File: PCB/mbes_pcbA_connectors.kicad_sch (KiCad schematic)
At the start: 14 parts

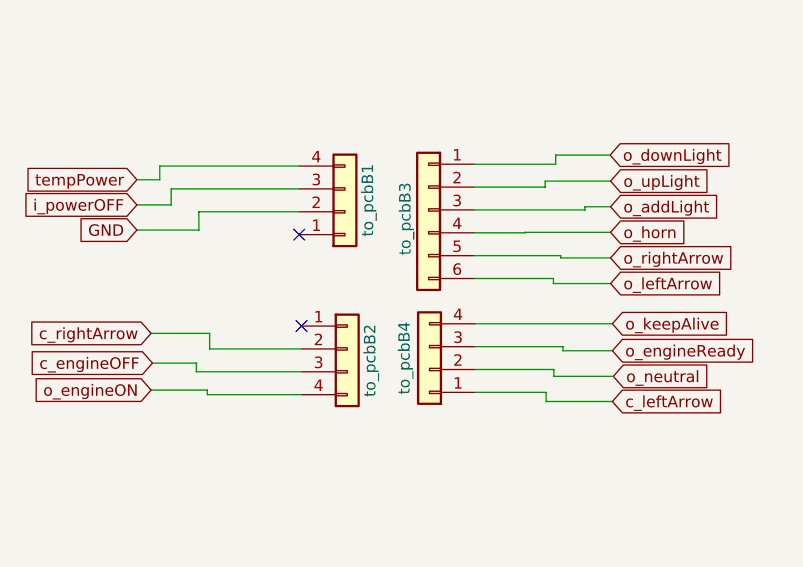
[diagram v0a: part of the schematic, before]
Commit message: Wrong connectors sizes fixed
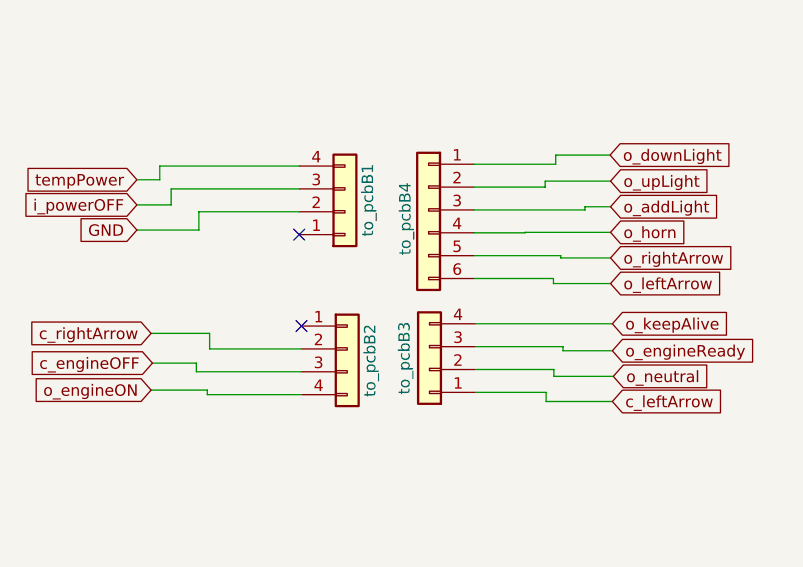
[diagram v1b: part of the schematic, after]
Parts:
- renumbered to_pcbB4 to to_pcbB3, to_pcbB3 to to_pcbB4
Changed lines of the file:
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@@
 		(on_board yes)
 		(dnp no)
-		(property "Reference" "to_pcbB4"
+		(property "Reference" "to_pcbB3"
 			(at 202.184 124.968 90)
 			(effects
@@
 			(project "pcb-a"
 				(path "/709d0967-afe5-49d3-92a5-d2bb94550bdb/0b22d592-b723-42a2-89dd-bec665c2bd26"
-					(reference "to_pcbB4")
+					(reference "to_pcbB3")
 					(unit 1)
 				)
@@
 		(on_board yes)
 		(dnp no)
-		(property "Reference" "to_pcbB3"
+		(property "Reference" "to_pcbB4"
 			(at 202.2856 113.538 90)
 			(effects
@@
 			(project "pcb-a"
 				(path "/709d0967-afe5-49d3-92a5-d2bb94550bdb/0b22d592-b723-42a2-89dd-bec665c2bd26"
-					(reference "to_pcbB3")
-					(unit 1)
-				)
+					(reference "to_pcbB4")
+					(unit 1)
+				)

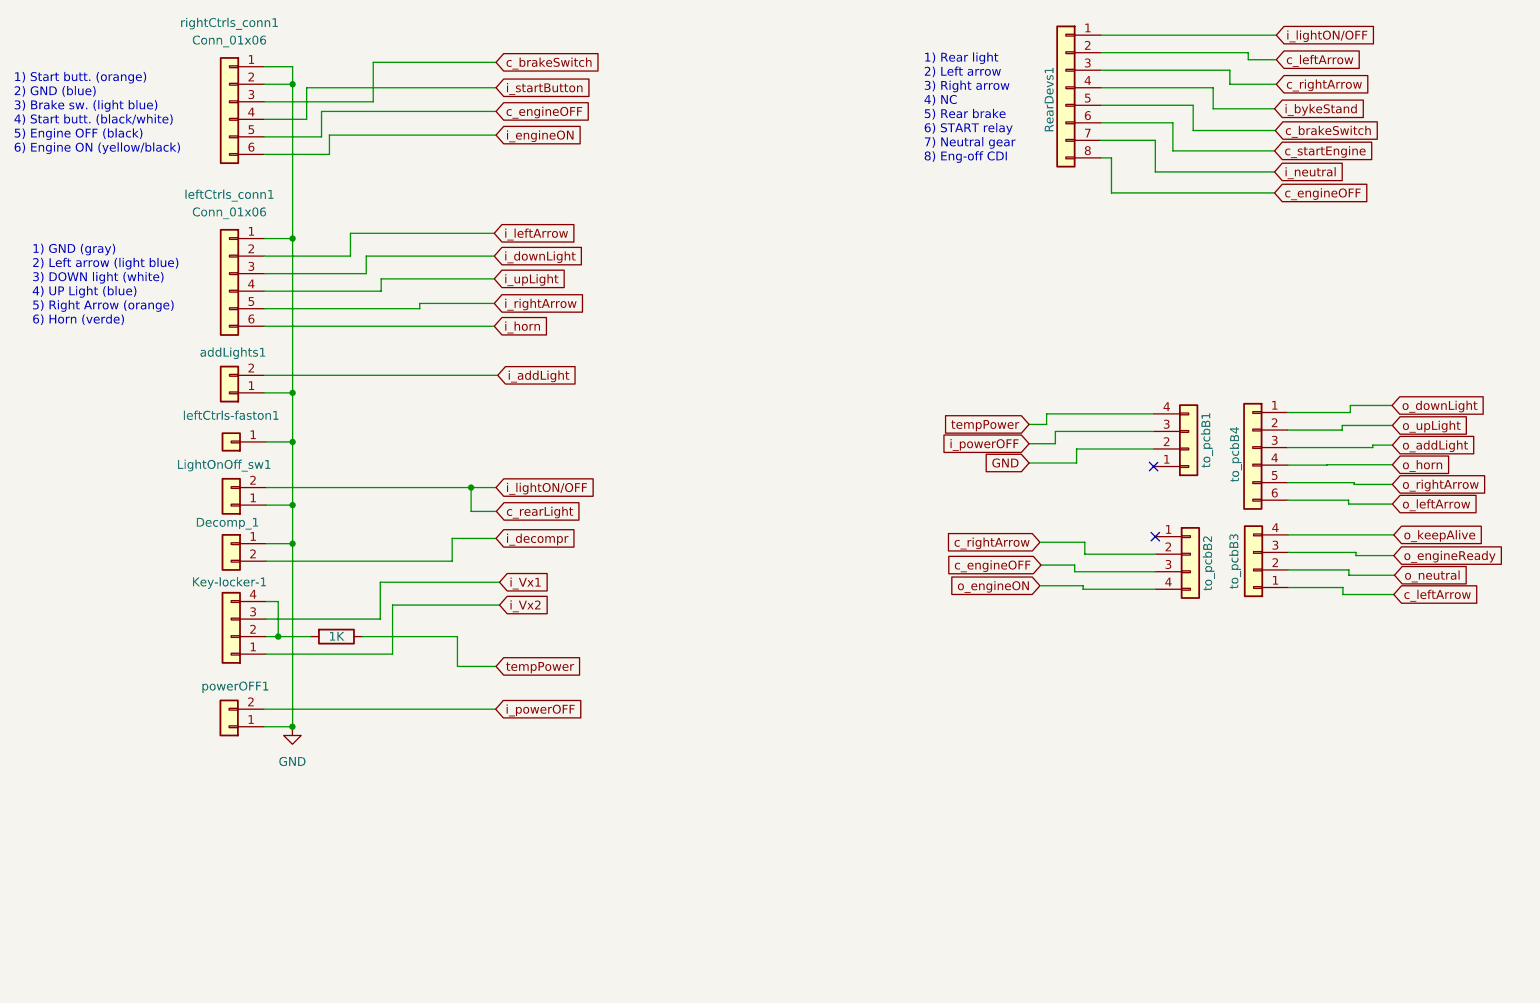
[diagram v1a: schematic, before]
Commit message: Parking button added and Horn management removed
Horn is connected directly to the power PCB
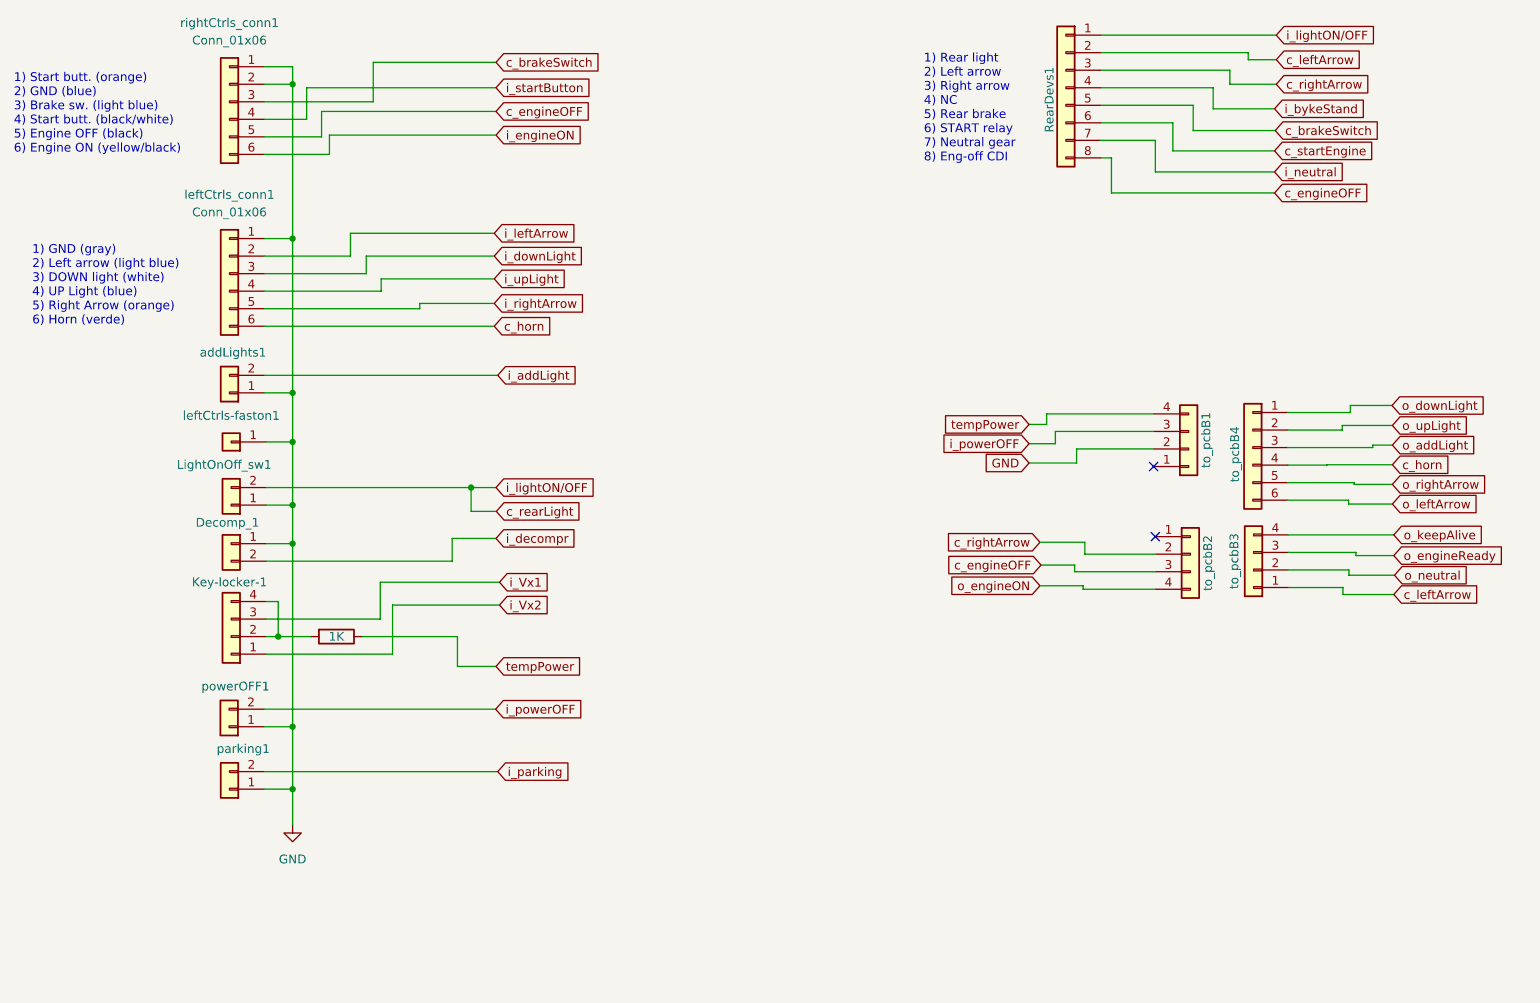
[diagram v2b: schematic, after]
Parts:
- added parking1: Conn_01x02, Connector_Wire:SolderWire-0.15sqmm_1x02_P4mm_D0.5mm_OD1.5mm, symbol Connector_Generic:Conn_01x02
- R1: footprint Resistor_THT:R_Axial_DIN0207_L6.3mm_D2.5mm_P7.62mm_Horizontal -> Resistor_THT:R_Axial_DIN0204_L3.6mm_D1.6mm_P5.08mm_Horizontal
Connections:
- net o_horn is gone; now on net c_horn: to_pcbB4.4 (Pin_4)
- net GND: now also parking1.1 (Pin_1)
- net i_horn renamed c_horn
- new net i_parking: parking1.2 (Pin_2)
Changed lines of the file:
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@@
 	)
 	(junction
+		(at 65.786 148.9456)
+		(diameter 0)
+		(color 0 0 0 0)
+	)
+	(junction
 		(at 65.786 122.428)
 		(diameter 0)
@@
 	)
 	(junction
-		(at 65.7606 148.9456)
+		(at 65.786 157.988)
 		(diameter 0)
 		(color 0 0 0 0)
@@
 	(wire
 		(pts
+			(xy 61.722 155.448) (xy 95.504 155.448)
+		)
+		(stroke
+			(width 0)
+			(type default)
+		)
+	)
+	(wire
+		(pts
 			(xy 208.1276 62.5856) (xy 196.2404 62.5856)
 		)
@@
 	(wire
 		(pts
+			(xy 61.722 157.988) (xy 65.786 157.988)
+		)
+		(stroke
+			(width 0)
+			(type default)
+		)
+	)
+	(wire
+		(pts
 			(xy 219.5576 113.8428) (xy 225.0948 113.8428)
 		)
@@
 	(wire
 		(pts
+			(xy 65.786 163.068) (xy 65.786 157.988)
+		)
+		(stroke
+			(width 0)
+			(type default)
+		)
+	)
+	(wire
+		(pts
 			(xy 209.9564 113.5888) (xy 219.5576 113.5888)
 		)
@@
 	(wire
 		(pts
-			(xy 65.7606 148.9456) (xy 65.786 148.9456)
-		)
-		(stroke
-			(width 0)
-			(type default)
-		)
-	)
-	(wire
-		(pts
 			(xy 180.2892 129.032) (xy 190.754 129.032)
 		)
@@
 	(wire
 		(pts
-			(xy 61.6712 148.9456) (xy 65.7606 148.9456)
+			(xy 61.6712 148.9456) (xy 65.786 148.9456)
 		)
 		(stroke
@@
 	(wire
 		(pts
+			(xy 65.786 157.988) (xy 65.786 148.9456)
+		)
+		(stroke
+			(width 0)
+			(type default)
+		)
+	)
+	(wire
+		(pts
 			(xy 201.549 53.848) (xy 201.549 55.88)
 		)
@@
 		)
 	)
-	(global_label "o_horn"
+	(global_label "c_horn"
 		(shape input)
 		(at 225.0948 110.998 0)
@@
 		)
 		(property "Intersheetrefs" "${INTERSHEET_REFS}"
-			(at 225.0948 110.998 0)
+			(at 234.3694 110.998 0)
 			(effects
 				(font
 					(size 1.27 1.27)
 				)
+				(justify left)
 				(hide yes)
 			)
 		)
 		(property "Riferimenti inter-foglio" "${INTERSHEET_REFS}"
-			(at 233.8579 110.9186 0)
+			(at 225.0948 113.1888 0)
 			(effects
 				(font
@@
 		)
 	)
-	(global_label "i_horn"
+	(global_label "c_horn"
 		(shape input)
 		(at 94.996 90.932 0)
@@
 		)
 		(property "Intersheetrefs" "${INTERSHEET_REFS}"
-			(at 94.996 90.932 0)
+			(at 104.2706 90.932 0)
 			(effects
 				(font
 					(size 1.27 1.27)
 				)
+				(justify left)
 				(hide yes)
 			)
 		)
 		(property "Riferimenti inter-foglio" "${INTERSHEET_REFS}"
-			(at 103.2148 90.8526 0)
+			(at 94.996 93.1228 0)
 			(effects
 				(font
@@
 		)
 	)
+	(global_label "i_parking"
+		(shape input)
+		(at 95.504 155.448 0)
+		(fields_autoplaced yes)
+		(effects
+			(font
+				(size 1.27 1.27)
+			)
+			(justify left)
+		)
+		(property "Intersheetrefs" "${INTERSHEET_REFS}"
+			(at 107.0767 155.448 0)
+			(effects
+				(font
+					(size 1.27 1.27)
+				)
+				(justify left)
+				(hide yes)
+			)
+		)
+		(property "Riferimenti inter-foglio" "${INTERSHEET_REFS}"
+			(at 95.504 157.6388 0)
+			(effects
+				(font
+					(size 1.27 1.27)
+				)
+				(justify left)
+				(hide yes)
+			)
+		)
+	)
 	(global_label "c_rearLight"
 		(shape input)
@@
 	(symbol
 		(lib_id "power:GND")
-		(at 65.7606 148.9456 0)
+		(at 65.786 163.068 0)
 		(unit 1)
 		(exclude_from_sim no)
@@
 		(fields_autoplaced yes)
 		(property "Reference" "#PWR0108"
-			(at 65.7606 155.2956 0)
+			(at 65.786 169.418 0)
 			(effects
 				(font
@@
 		)
 		(property "Value" "GND"
-			(at 65.7606 154.0256 0)
+			(at 65.786 168.148 0)
 			(effects
 				(font
@@
 		)
 		(property "Footprint" ""
-			(at 65.7606 148.9456 0)
+			(at 65.786 163.068 0)
 			(effects
 				(font
@@
 		)
 		(property "Datasheet" ""
-			(at 65.7606 148.9456 0)
+			(at 65.786 163.068 0)
 			(effects
 				(font
@@
 		)
 		(property "Description" ""
-			(at 65.7606 148.9456 0)
+			(at 65.786 163.068 0)
 			(effects
 				(font
@@
 	)
 	(symbol
+		(lib_id "Connector_Generic:Conn_01x02")
+		(at 56.642 157.988 180)
+		(unit 1)
+		(exclude_from_sim no)
+		(in_bom yes)
+		(on_board yes)
+		(dnp no)
+		(property "Reference" "parking1"
+			(at 62.484 152.146 0)
+			(effects
+				(font
+					(size 1.27 1.27)
+				)
+				(justify left)
+			)
+		)
+		(property "Value" "Conn_01x02"
+			(at 55.3721 160.528 90)
+			(effects
+				(font
+					(size 1.27 1.27)
+				)
+				(justify left)
+				(hide yes)
+			)
+		)
+		(property "Footprint" "Connector_Wire:SolderWire-0.15sqmm_1x02_P4mm_D0.5mm_OD1.5mm"
+			(at 56.642 157.988 0)
+			(effects
+				(font
+					(size 1.27 1.27)
+				)
+				(hide yes)
+			)
+		)
+		(property "Datasheet" "~"
+			(at 56.642 157.988 0)
+			(effects
+				(font
+					(size 1.27 1.27)
+				)
+				(hide yes)
+			)
+		)
+		(property "Description" ""
+			(at 56.642 157.988 0)
+			(effects
+				(font
+					(size 1.27 1.27)
+				)
+				(hide yes)
+			)
+		)
+		(pin "1"
+		)
+		(pin "2"
+		)
+		(instances
+			(project "pcb-a"
+				(path "/709d0967-afe5-49d3-92a5-d2bb94550bdb/0b22d592-b723-42a2-89dd-bec665c2bd26"
+					(reference "parking1")
+					(unit 1)
+				)
+			)
+		)
+	)
+	(symbol
 		(lib_id "Connector_Generic:Conn_01x04")
 		(at 195.834 123.952 0)
@@
 			)
 		)
-		(property "Footprint" "Resistor_THT:R_Axial_DIN0207_L6.3mm_D2.5mm_P7.62mm_Horizontal"
+		(property "Footprint" "Resistor_THT:R_Axial_DIN0204_L3.6mm_D1.6mm_P5.08mm_Horizontal"
 			(at 72.136 134.112 90)
 			(effects

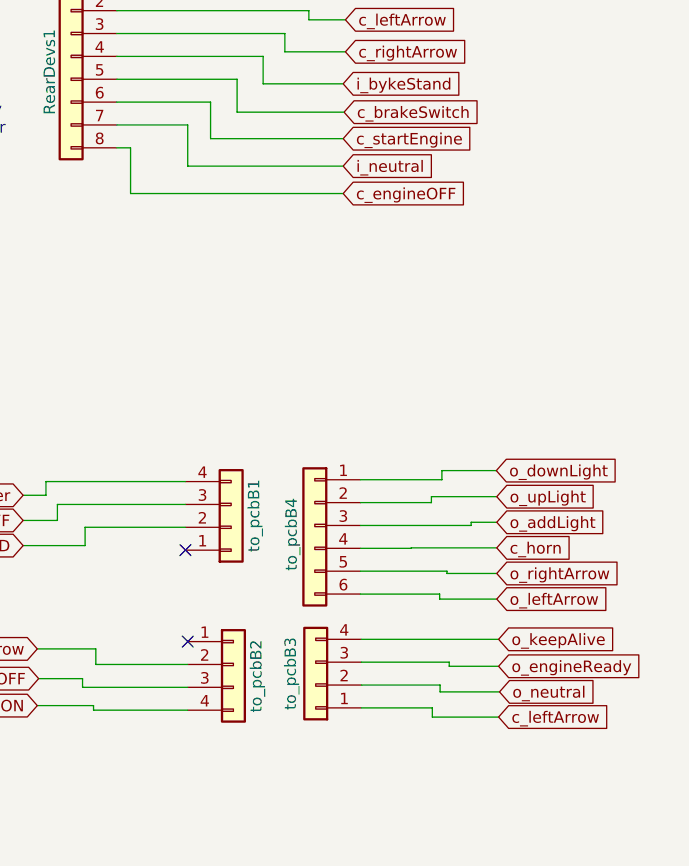
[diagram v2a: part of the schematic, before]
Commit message: o_NEUTRAL is connected directly to the led
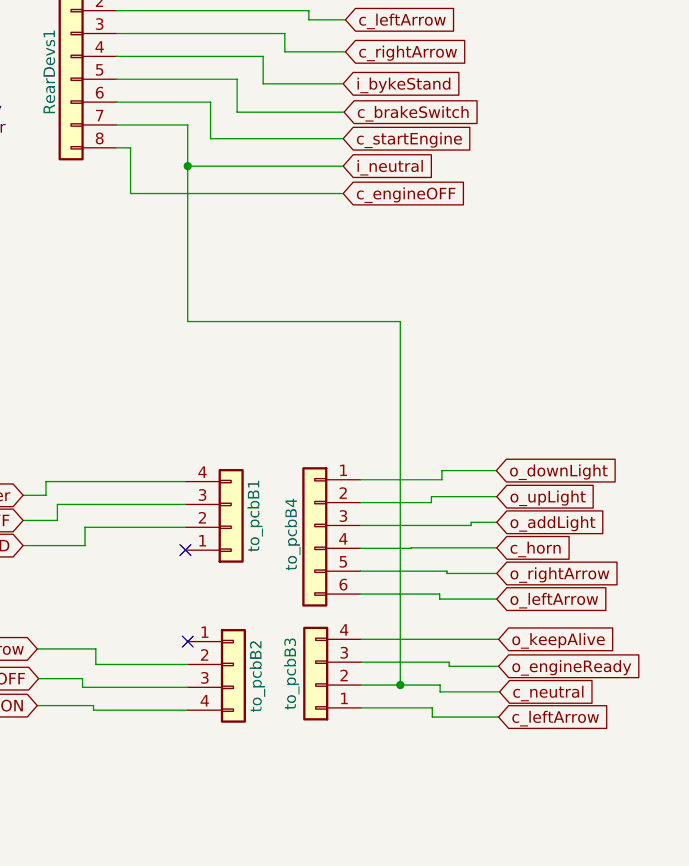
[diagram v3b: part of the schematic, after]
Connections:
- net o_neutral is gone; now on net c_neutral: to_pcbB3.2 (Pin_2)
- net i_neutral renamed c_neutral
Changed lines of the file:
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@@
+	)
+	(junction
+		(at 214.376 126.238)
+		(diameter 0)
+		(color 0 0 0 0)
 	)
 	(junction
@@
 	)
 	(junction
+		(at 190.754 68.58)
+		(diameter 0)
+		(color 0 0 0 0)
+	)
+	(junction
 		(at 91.6432 114.3)
 		(diameter 0)
@@
 	(wire
 		(pts
+			(xy 214.376 126.238) (xy 210.058 126.238)
+		)
+		(stroke
+			(width 0)
+			(type default)
+		)
+	)
+	(wire
+		(pts
 			(xy 180.2892 129.032) (xy 190.754 129.032)
 		)
@@
 	(wire
 		(pts
-			(xy 218.7956 126.238) (xy 210.058 126.238)
+			(xy 214.376 85.852) (xy 190.754 85.852)
+		)
+		(stroke
+			(width 0)
+			(type default)
+		)
+	)
+	(wire
+		(pts
+			(xy 218.7956 126.238) (xy 214.376 126.238)
 		)
 		(stroke
@@
 	(wire
 		(pts
+			(xy 190.754 85.852) (xy 190.754 68.58)
+		)
+		(stroke
+			(width 0)
+			(type default)
+		)
+	)
+	(wire
+		(pts
 			(xy 61.722 58.42) (xy 77.47 58.42)
 		)
@@
 		(pts
 			(xy 172.466 107.95) (xy 176.276 107.95)
+		)
+		(stroke
+			(width 0)
+			(type default)
+		)
+	)
+	(wire
+		(pts
+			(xy 214.376 126.238) (xy 214.376 85.852)
 		)
 		(stroke
@@
 		)
 	)
-	(global_label "o_neutral"
+	(global_label "c_neutral"
 		(shape input)
 		(at 225.3996 127 0)
@@
 		)
 		(property "Intersheetrefs" "${INTERSHEET_REFS}"
-			(at 225.3996 127 0)
-			(effects
-				(font
-					(size 1.27 1.27)
-				)
+			(at 237.1537 127 0)
+			(effects
+				(font
+					(size 1.27 1.27)
+				)
+				(justify left)
 				(hide yes)
 			)
 		)
 		(property "Riferimenti inter-foglio" "${INTERSHEET_REFS}"
-			(at 236.6422 126.9206 0)
-			(effects
-				(font
+			(at 225.3996 129.1908 0)
+			(effects
+				(font
